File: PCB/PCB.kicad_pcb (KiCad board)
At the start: 2 copper layers, 101.6 x 39.7 mm, 32 parts, among them SW1 SW_Push, U1 ATmega32U4-AU, Y1 16MHz

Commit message: finished PCB?
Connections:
- USB1 pad 6: Net-(USB1-Pad6) -> GND
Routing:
- net GND: track 125.4 -> 144.5 mm
- added copper zone on B.Cu, net GND
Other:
- outline, holes or cut-outs redrawn
- board text added: "Designed by Ryan Yeung :)"

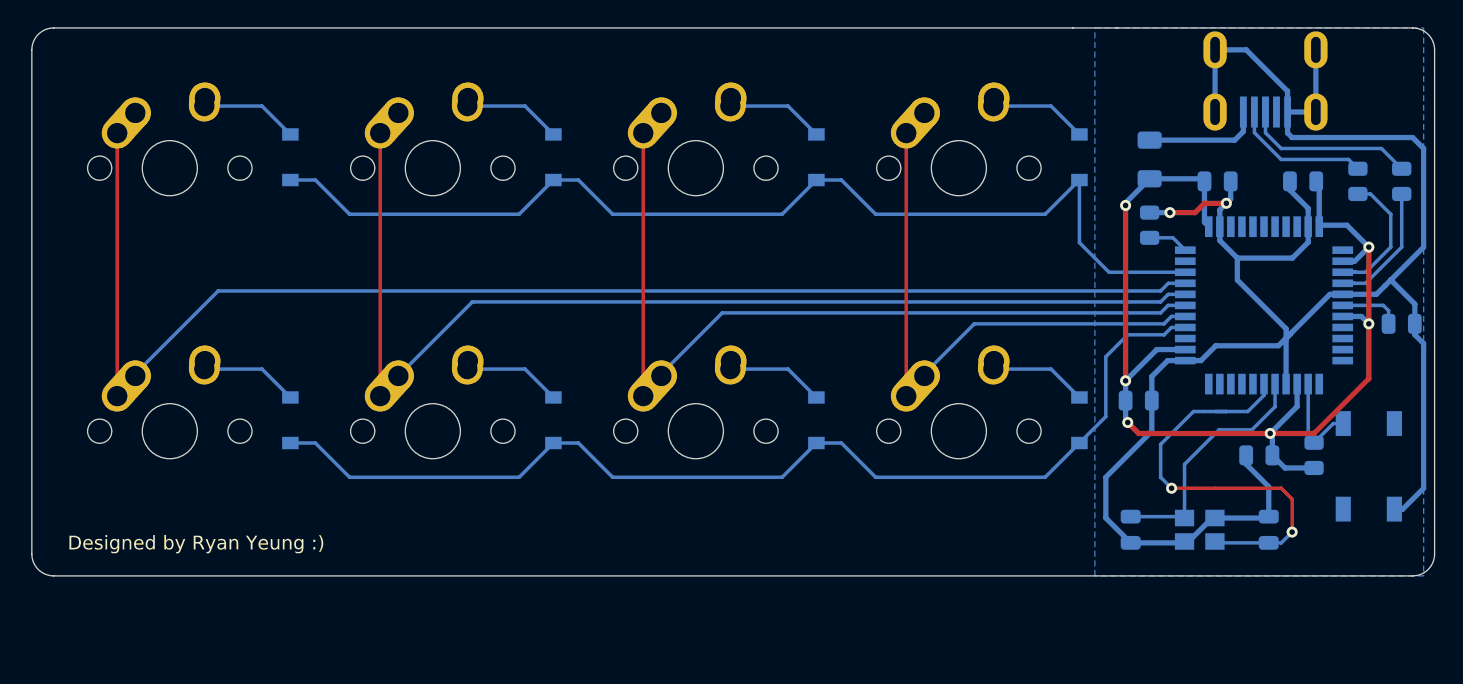
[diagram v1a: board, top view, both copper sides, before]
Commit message: added through-holes
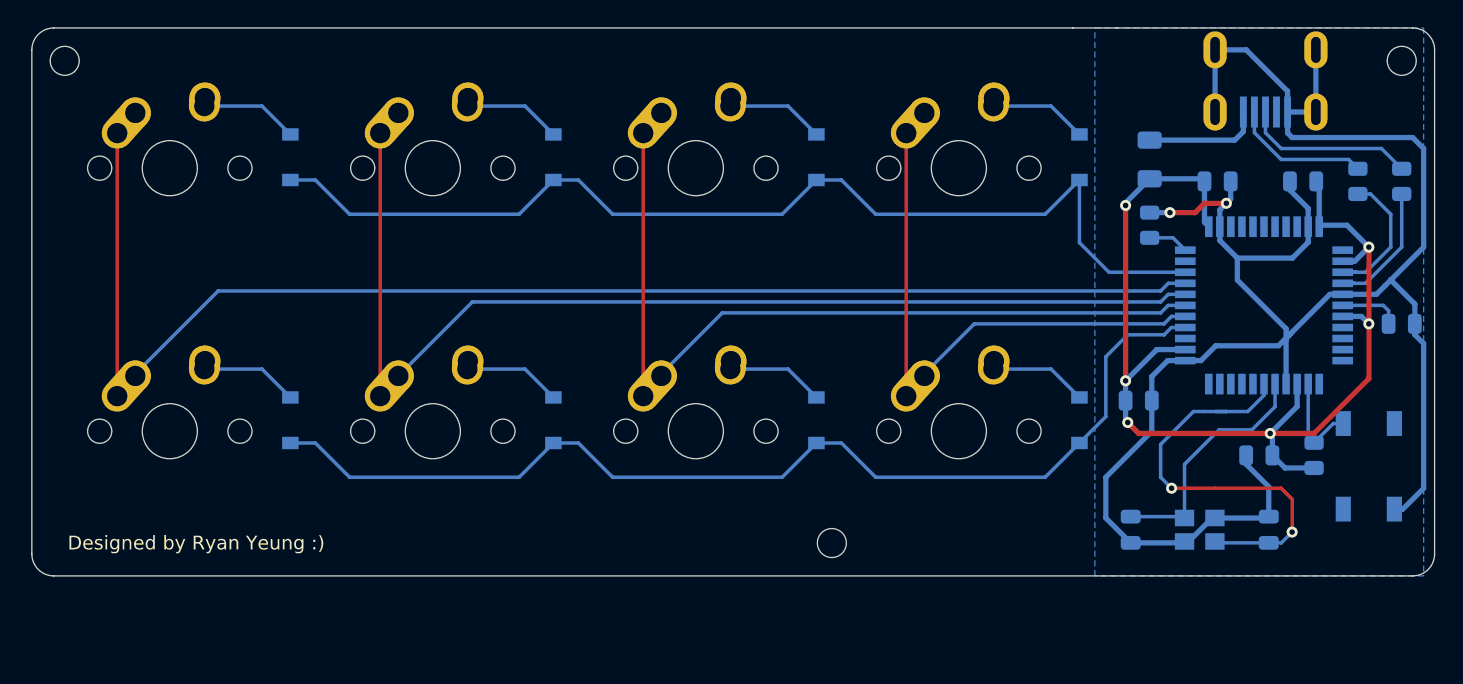
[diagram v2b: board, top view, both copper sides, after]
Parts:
- added REF**: MountingHole_2.1mm, MountingHole:MountingHole_2.1mm, F.Cu at (178.6, 105.6)
- added REF**: MountingHole_2.1mm, MountingHole:MountingHole_2.1mm, F.Cu at (123.0, 70.6)
- added REF**: MountingHole_2.1mm, MountingHole:MountingHole_2.1mm, F.Cu at (219.9, 70.6)

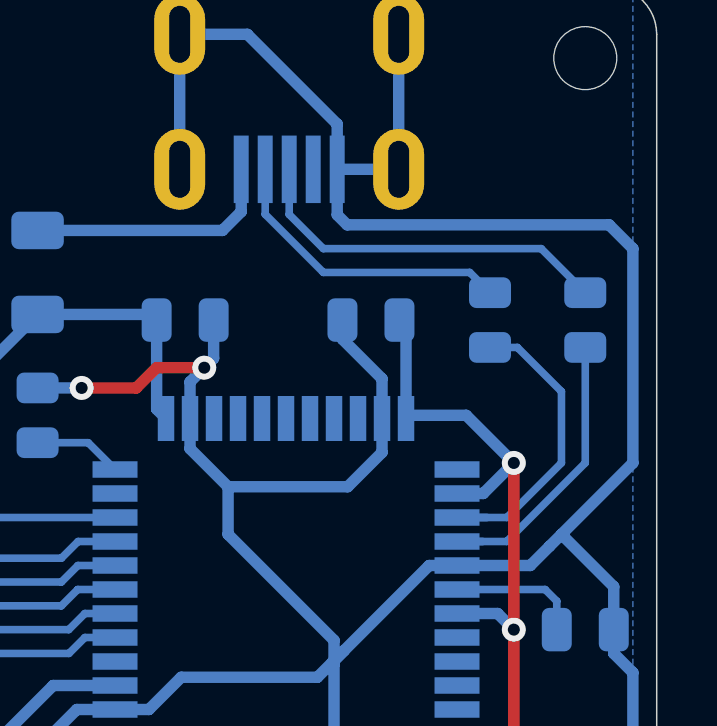
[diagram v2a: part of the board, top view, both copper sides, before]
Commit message: rerouted usb to make more parallel
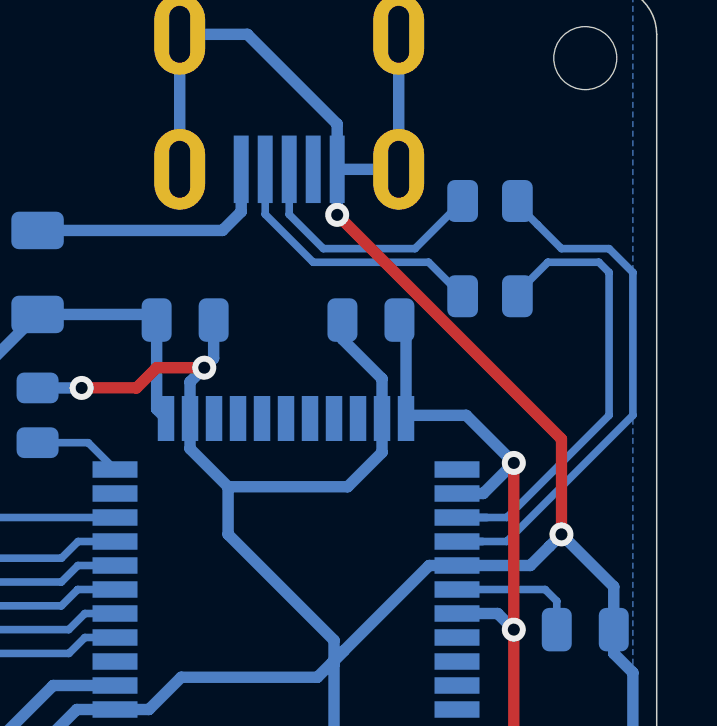
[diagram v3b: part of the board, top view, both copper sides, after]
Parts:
- moved R2 5.08 mm to (216.7, 75.4), turned to 180 degrees
- moved R1 0.79 mm to (216.7, 78.6), turned to 180 degrees
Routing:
- net Net-(R2-Pad1): track 10.2 -> 18.1 mm
- net GND: track 144.5 -> 137.4 mm, vias 2 -> 4
- net Net-(R1-Pad1): track 10.6 -> 16.0 mm
- net D+: track 12.5 -> 8.42 mm
- net D-: track 10.1 -> 9.48 mm

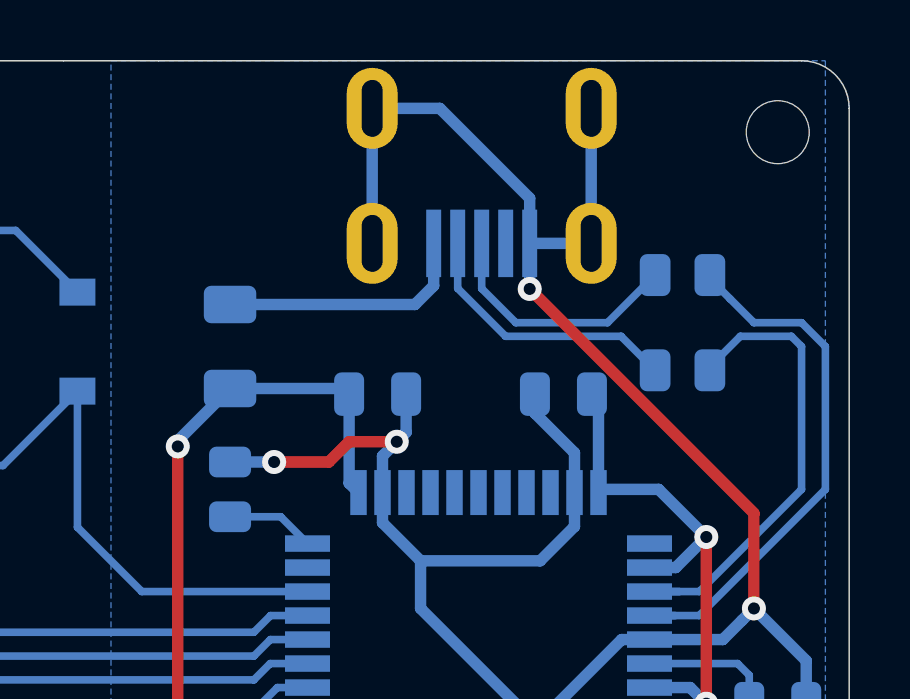
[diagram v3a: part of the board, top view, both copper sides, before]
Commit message: major changes: replaced usb with usb type C
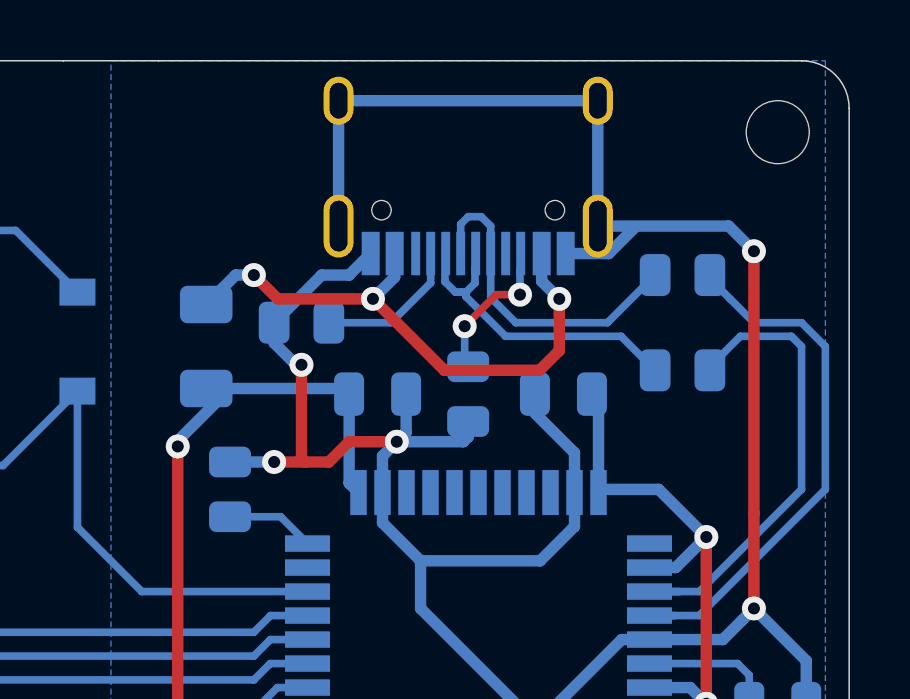
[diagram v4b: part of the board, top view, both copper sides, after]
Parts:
- removed USB1: Molex-0548190589, random-keyboard-parts:Molex-0548190589
- added J1: USB_C_Receptacle_USB2.0, Connector_USB:USB_C_Receptacle_HRO_TYPE-C-31-M-12, B.Cu at (209.6, 70.6)
- added R5: 5.1k, Resistor_SMD:R_0805_2012Metric, B.Cu at (209.6, 79.4)
- added R6: 5.1k, Resistor_SMD:R_0805_2012Metric, B.Cu at (204.0, 77.0)
- moved F1 0.79 mm to (200.8, 77.8)
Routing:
- net GND: track 137.4 -> 152.1 mm, vias 4 -> 5
- net VCC: track 8.46 -> 19.1 mm, vias 0 -> 3
- net Net-(J1-PadB5): track 0.00 -> 5.06 mm, vias 0 -> 2
- net Net-(J1-PadA5): track 0.00 -> 4.92 mm
- net D+: track 8.42 -> 11.1 mm
- net D-: track 9.48 -> 10.2 mm

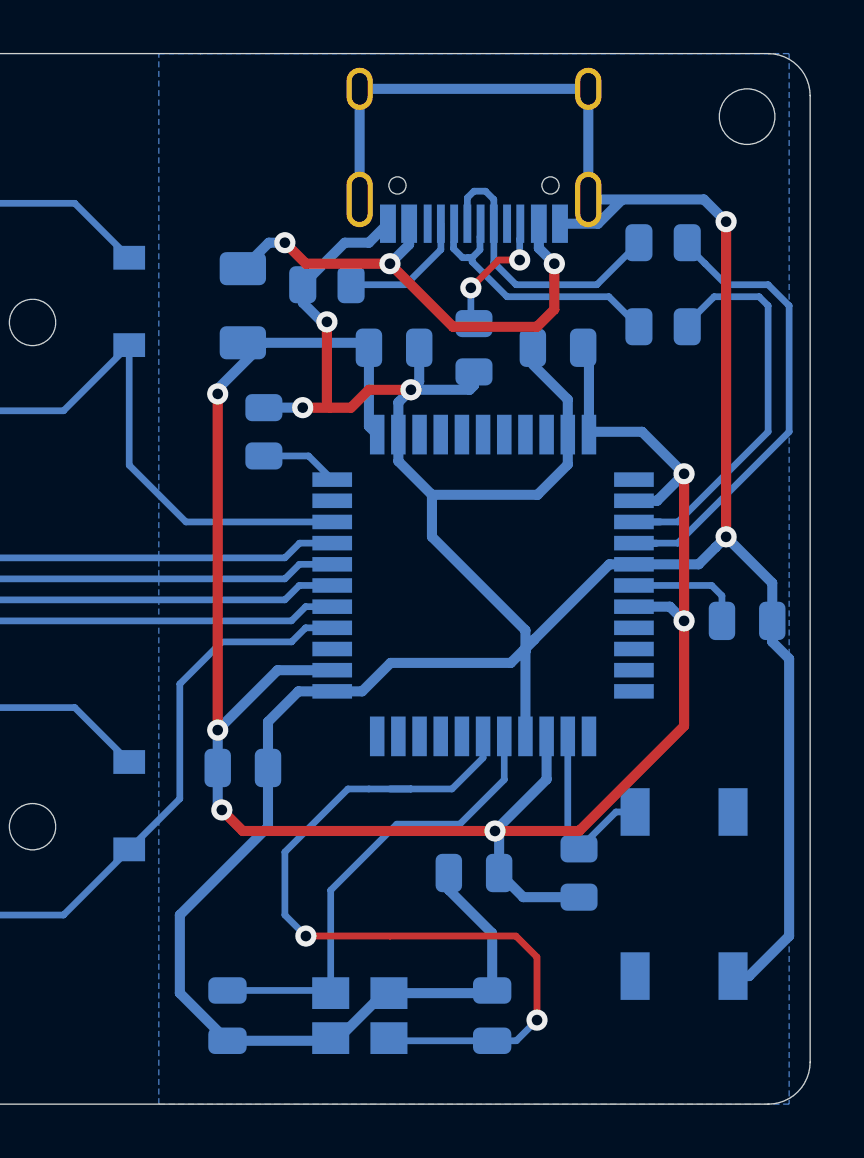
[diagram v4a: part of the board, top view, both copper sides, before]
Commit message: replaced usb footprint with GCT-usb4085 available in digikey
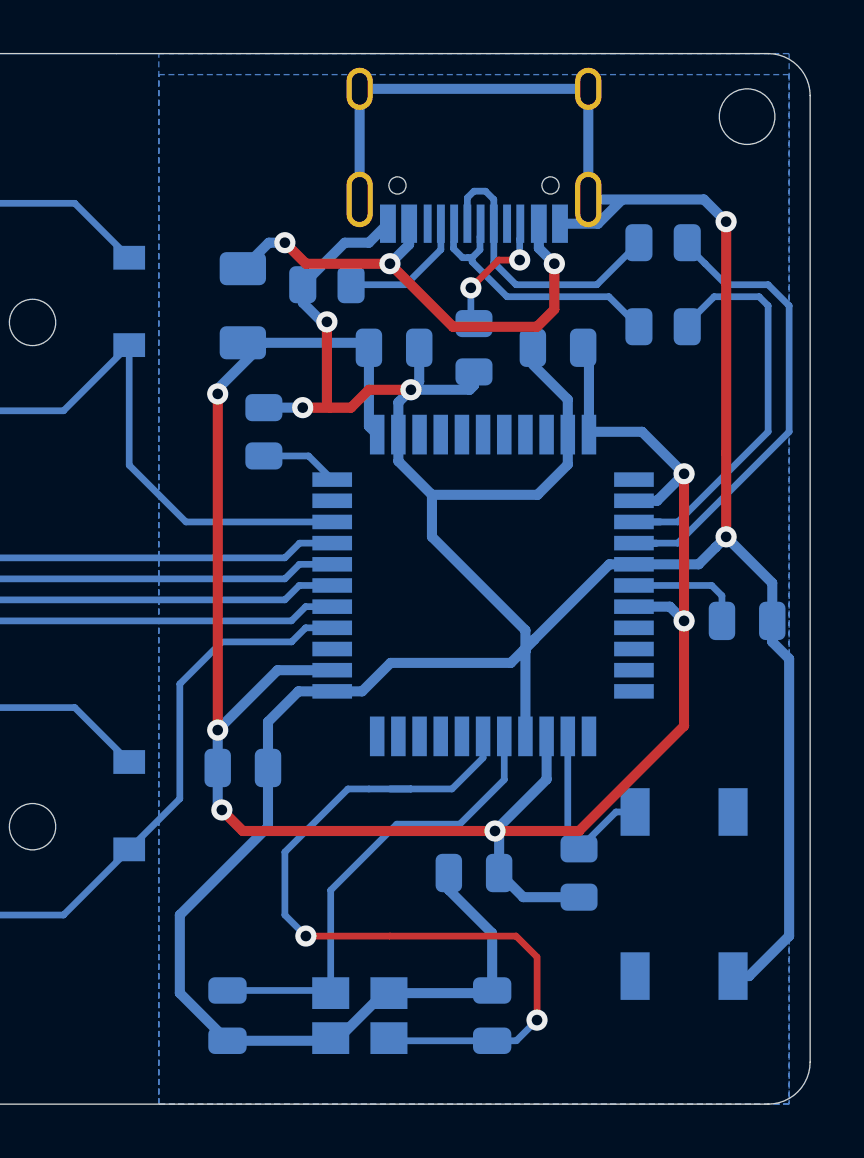
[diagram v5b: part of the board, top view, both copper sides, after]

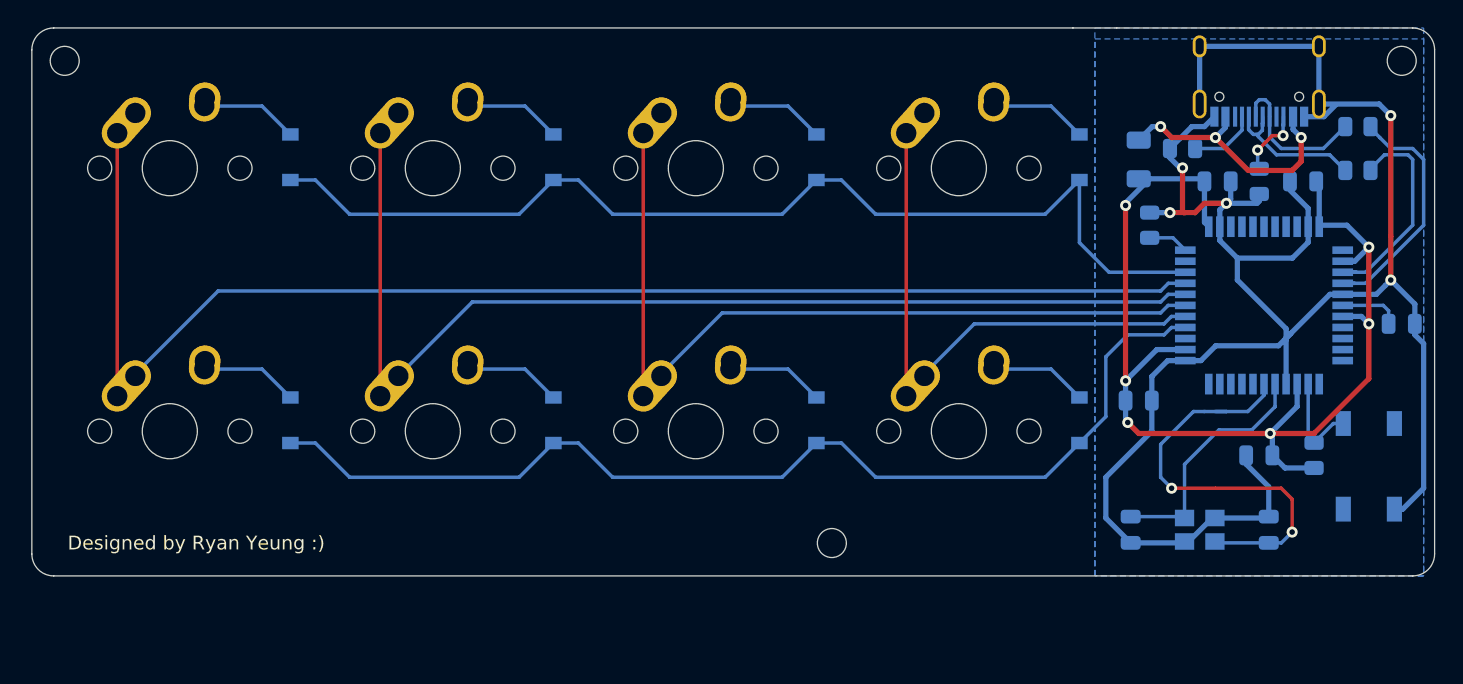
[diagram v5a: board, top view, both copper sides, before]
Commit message: added case and updated usb-c footprint
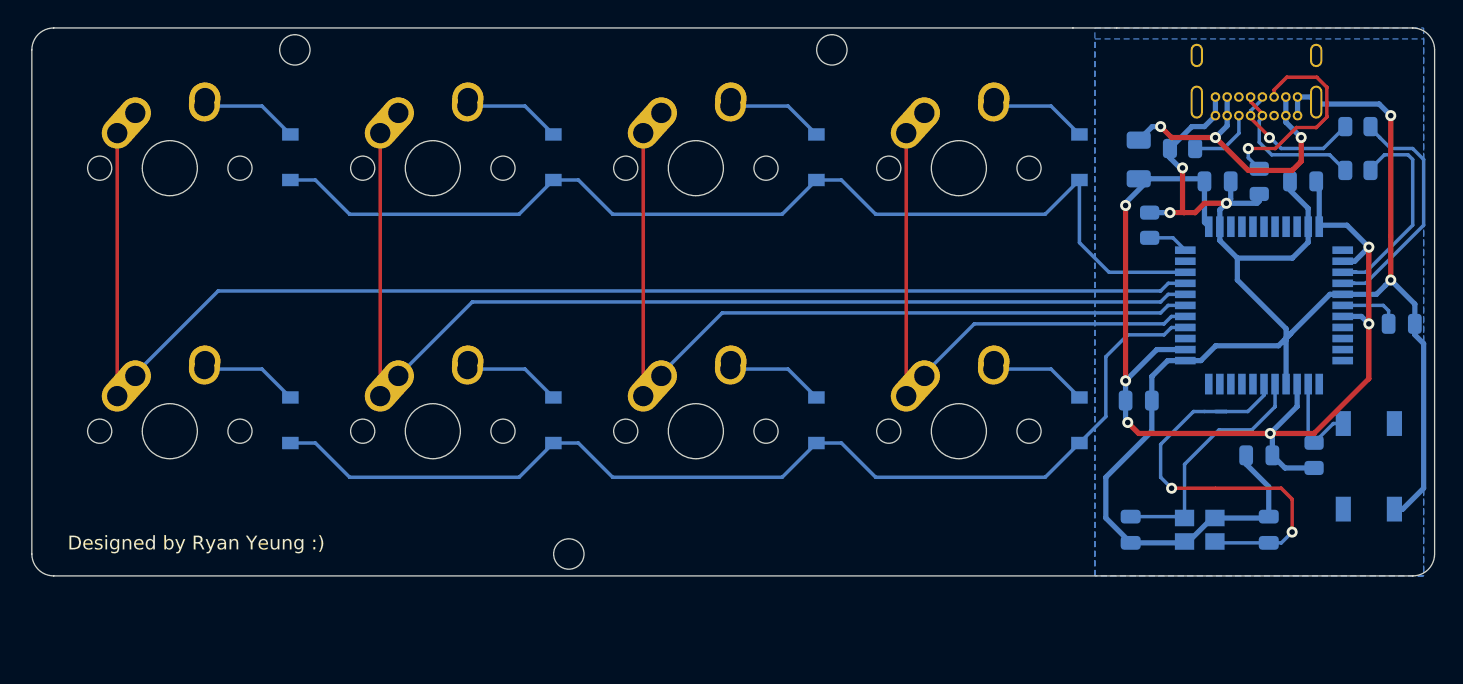
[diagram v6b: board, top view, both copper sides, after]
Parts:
- removed the REF** at (178.6, 105.6)
- removed the REF** at (123.0, 70.6)
- removed the REF** at (219.9, 70.6)
- added ?: , , F.Cu at (126.2, 104.8)
- added REF**: MountingHole_2.2mm_M2, MountingHole:MountingHole_2.2mm_M2, F.Cu at (159.5, 106.4)
- added REF**: MountingHole_2.2mm_M2, MountingHole:MountingHole_2.2mm_M2, F.Cu at (178.6, 69.8)
- added REF**: MountingHole_2.2mm_M2, MountingHole:MountingHole_2.2mm_M2, F.Cu at (139.7, 69.8)
- J1: footprint Connector_USB:USB_C_Receptacle_HRO_TYPE-C-31-M-12 -> Connector_USB:USB_C_Receptacle_GCT_USB4085
- moved J1 5.08 mm to (206.4, 74.6)
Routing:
- net GND: track 152.1 -> 136.7 mm
- net Net-(J1-PadB5): track 5.06 -> 15.8 mm, vias 2 -> 1
- net VCC: track 19.1 -> 22.2 mm
- net D-: track 10.2 -> 11.1 mm
- net D+: track 11.1 -> 10.4 mm, vias 0 -> 1
